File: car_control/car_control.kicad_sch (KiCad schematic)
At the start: 30 parts, among them J1 Screw_Terminal_01x02, J2 Conn_01x03, J3 Conn_01x03, J4 Screw_Terminal_01x02, Q1 IRF540N, Q2 2N3904, SW1 SW_SPST, SW2 SW_Push, U1 TCRT5000

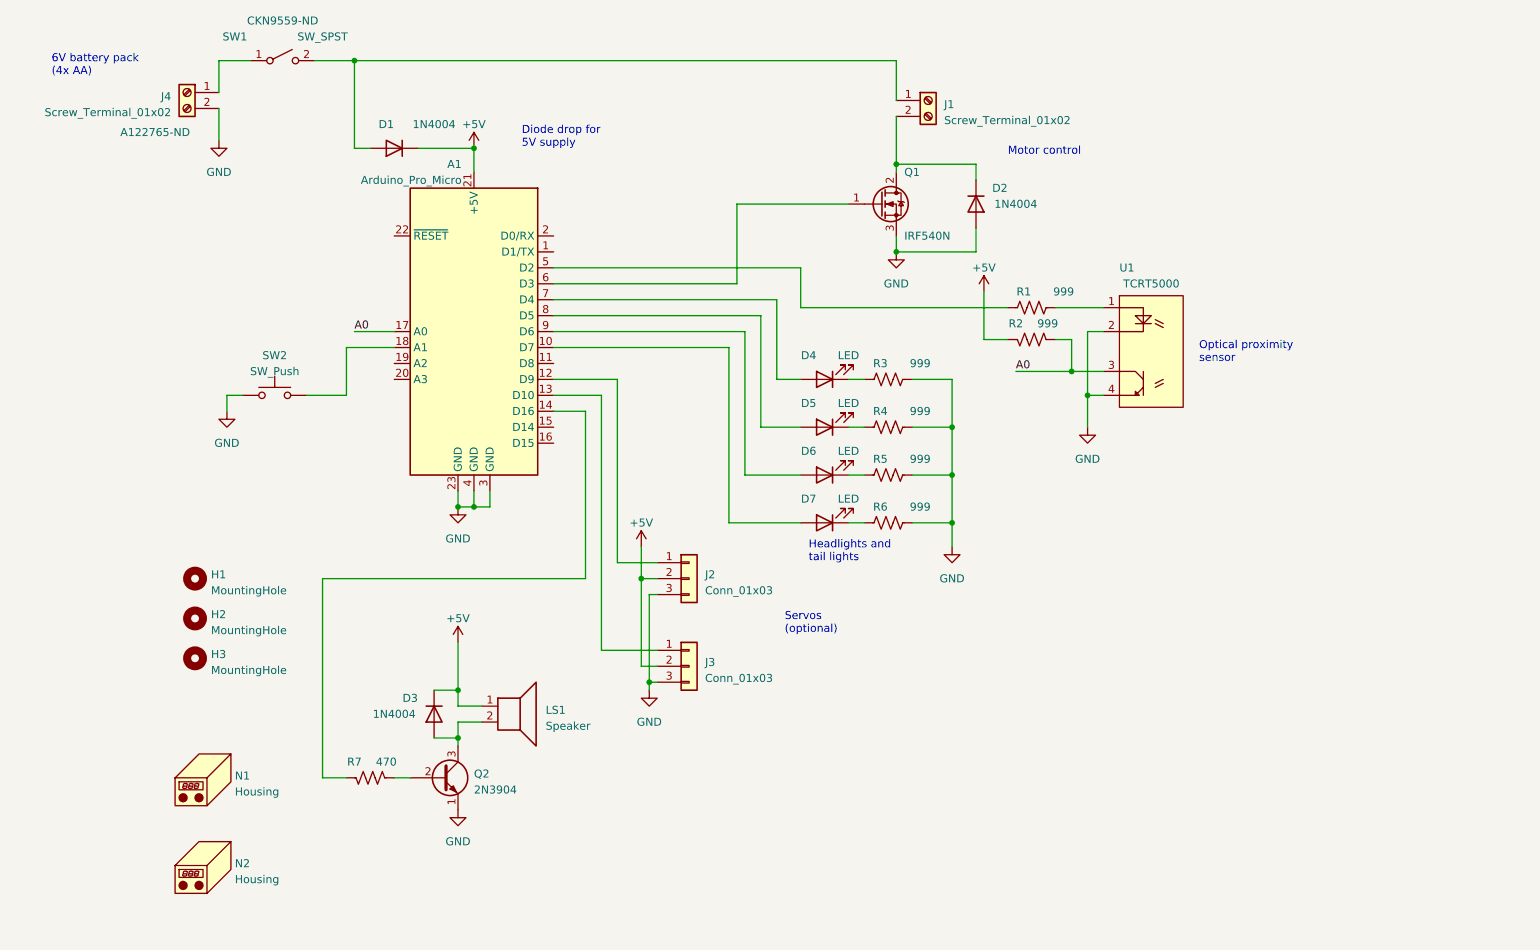
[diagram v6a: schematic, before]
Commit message: Add USB serial connector
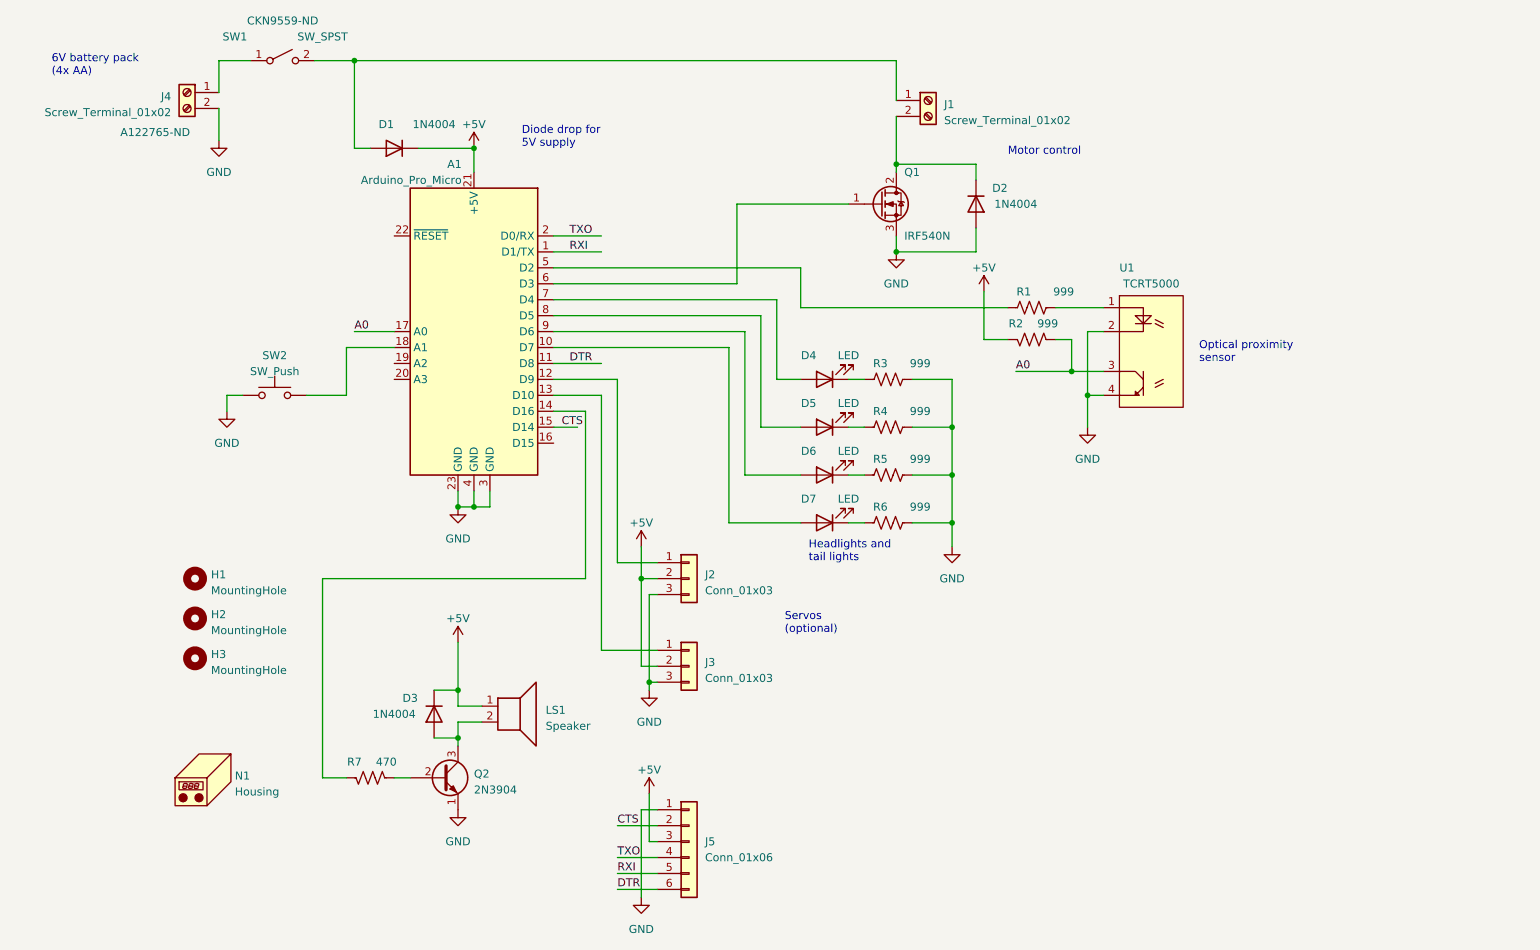
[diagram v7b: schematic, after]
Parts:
- removed N2: Housing, car_as:car_as, symbol Mechanical:Housing
- added J5: Conn_01x06, Connector_PinHeader_2.54mm:PinHeader_1x06_P2.54mm_Vertical, symbol Connector_Generic:Conn_01x06
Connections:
- net +5V: now also J5.3 (Pin_3)
- net GND: now also J5.1 (Pin_1)
- net RXI: now reaches A1.1 (D1/TX)
- net RXI: now also J5.5 (Pin_5)
- net DTR: now reaches A1.11 (D8)
- net DTR: now also J5.6 (Pin_6)
- net CTS: now reaches A1.15 (D14)
- net CTS: now also J5.2 (Pin_2)
- net TXO: now reaches A1.2 (D0/RX)
- net TXO: now also J5.4 (Pin_4)
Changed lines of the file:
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@@
   (junction (at 116.84 146.05) (diameter 0) (color 0 0 0 0)
   )
+  (wire (pts (xy 101.6 95.25) (xy 109.22 95.25))
+    (stroke (width 0) (type default))
+  )
   (wire (pts (xy 148.59 97.79) (xy 151.13 97.79))
     (stroke (width 0) (type default))
@@
     (stroke (width 0) (type default))
   )
+  (wire (pts (xy 116.84 163.83) (xy 116.84 171.45))
+    (stroke (width 0) (type default))
+  )
   (wire (pts (xy 49.53 100.33) (xy 49.53 102.87))
     (stroke (width 0) (type default))
@@
     (stroke (width 0) (type default))
   )
+  (wire (pts (xy 116.84 171.45) (xy 118.11 171.45))
+    (stroke (width 0) (type default))
+  )
   (wire (pts (xy 134.62 105.41) (xy 140.97 105.41))
     (stroke (width 0) (type default))
@@
     (stroke (width 0) (type default))
   )
+  (wire (pts (xy 115.57 166.37) (xy 118.11 166.37))
+    (stroke (width 0) (type default))
+  )
+  (wire (pts (xy 111.76 168.91) (xy 118.11 168.91))
+    (stroke (width 0) (type default))
+  )
+  (wire (pts (xy 101.6 77.47) (xy 109.22 77.47))
+    (stroke (width 0) (type default))
+  )
   (wire (pts (xy 130.81 69.85) (xy 130.81 82.55))
     (stroke (width 0) (type default))
@@
     (stroke (width 0) (type default))
   )
+  (wire (pts (xy 101.6 105.41) (xy 105.41 105.41))
+    (stroke (width 0) (type default))
+  )
   (wire (pts (xy 168.91 66.04) (xy 168.91 63.5))
     (stroke (width 0) (type default))
@@
     (stroke (width 0) (type default))
   )
+  (wire (pts (xy 115.57 180.34) (xy 115.57 166.37))
+    (stroke (width 0) (type default))
+  )
   (wire (pts (xy 69.85 90.17) (xy 76.2 90.17))
     (stroke (width 0) (type default))
@@
     (stroke (width 0) (type default))
   )
+  (wire (pts (xy 111.76 176.53) (xy 118.11 176.53))
+    (stroke (width 0) (type default))
+  )
+  (wire (pts (xy 101.6 74.93) (xy 109.22 74.93))
+    (stroke (width 0) (type default))
+  )
+  (wire (pts (xy 111.76 179.07) (xy 118.11 179.07))
+    (stroke (width 0) (type default))
+  )
   (wire (pts (xy 158.75 120.65) (xy 165.1 120.65))
     (stroke (width 0) (type default))
@@
     (stroke (width 0) (type default))
   )
+  (wire (pts (xy 111.76 173.99) (xy 118.11 173.99))
+    (stroke (width 0) (type default))
+  )
   (wire (pts (xy 111.76 97.79) (xy 111.76 127))
     (stroke (width 0) (type default))
@@
     (effects (font (size 1.27 1.27)) (justify left bottom))
   )
+  (label "DTR" (at 111.76 179.07 0) (fields_autoplaced)
+    (effects (font (size 1.27 1.27)) (justify left bottom))
+  )
+  (label "CTS" (at 111.76 168.91 0) (fields_autoplaced)
+    (effects (font (size 1.27 1.27)) (justify left bottom))
+  )
+  (label "TXO" (at 104.14 74.93 0) (fields_autoplaced)
+    (effects (font (size 1.27 1.27)) (justify left bottom))
+  )
+  (label "TXO" (at 111.76 173.99 0) (fields_autoplaced)
+    (effects (font (size 1.27 1.27)) (justify left bottom))
+  )
+  (label "CTS" (at 102.87 105.41 0) (fields_autoplaced)
+    (effects (font (size 1.27 1.27)) (justify left bottom))
+  )
   (label "A0" (at 175.26 96.52 0) (fields_autoplaced)
+    (effects (font (size 1.27 1.27)) (justify left bottom))
+  )
+  (label "RXI" (at 111.76 176.53 0) (fields_autoplaced)
+    (effects (font (size 1.27 1.27)) (justify left bottom))
+  )
+  (label "DTR" (at 104.14 95.25 0) (fields_autoplaced)
+    (effects (font (size 1.27 1.27)) (justify left bottom))
+  )
+  (label "RXI" (at 104.14 77.47 0) (fields_autoplaced)
     (effects (font (size 1.27 1.27)) (justify left bottom))
   )
@@
     )
   )
+  (symbol (lib_id "power:+5V") (at 116.84 163.83 0) (mirror y) (unit 1)
+    (in_bom yes) (on_board yes) (dnp no) (fields_autoplaced)
+    (property "Reference" "#PWR013" (at 116.84 167.64 0)
+      (effects (font (size 1.27 1.27)) hide)
+    )
+    (property "Value" "+5V" (at 116.84 160.02 0)
+      (effects (font (size 1.27 1.27)))
+    )
+    (property "Footprint" "" (at 116.84 163.83 0)
+      (effects (font (size 1.27 1.27)) hide)
+    )
+    (property "Datasheet" "" (at 116.84 163.83 0)
+      (effects (font (size 1.27 1.27)) hide)
+    )
+    (pin "1")
+    (instances
+      (project "car_control"
+        (path "/08ff0388-b5fa-44e5-b165-5596a9674913"
+          (reference "#PWR013") (unit 1)
+        )
+      )
+    )
+  )
   (symbol (lib_id "Connector_Generic:Conn_01x03") (at 123.19 129.54 0) (unit 1)
     (in_bom yes) (on_board yes) (dnp no) (fields_autoplaced)
@@
     )
   )
-  (symbol (lib_id "Mechanical:Housing") (at 46.99 175.26 0) (unit 1)
-    (in_bom yes) (on_board yes) (dnp no) (fields_autoplaced)
-    (property "Reference" "N2" (at 50.8 174.9425 0)
-      (effects (font (size 1.27 1.27)) (justify left))
-    )
-    (property "Value" "Housing" (at 50.8 177.4825 0)
-      (effects (font (size 1.27 1.27)) (justify left))
-    )
-    (property "Footprint" "car_as:car_as" (at 48.26 173.99 0)
-      (effects (font (size 1.27 1.27)) hide)
-    )
-    (property "Datasheet" "~" (at 48.26 173.99 0)
-      (effects (font (size 1.27 1.27)) hide)
-    )
-    (instances
-      (project "car_control"
-        (path "/08ff0388-b5fa-44e5-b165-5596a9674913"
-          (reference "N2") (unit 1)
-        )
-      )
-    )
-  )
   (symbol (lib_id "Device:R_US") (at 154.94 120.65 90) (unit 1)
     (in_bom yes) (on_board yes) (dnp no)
@@
     )
   )
+  (symbol (lib_id "power:GND") (at 115.57 180.34 0) (unit 1)
+    (in_bom yes) (on_board yes) (dnp no) (fields_autoplaced)
+    (property "Reference" "#PWR014" (at 115.57 186.69 0)
+      (effects (font (size 1.27 1.27)) hide)
+    )
+    (property "Value" "GND" (at 115.57 185.42 0)
+      (effects (font (size 1.27 1.27)))
+    )
+    (property "Footprint" "" (at 115.57 180.34 0)
+      (effects (font (size 1.27 1.27)) hide)
+    )
+    (property "Datasheet" "" (at 115.57 180.34 0)
+      (effects (font (size 1.27 1.27)) hide)
+    )
+    (pin "1")
+    (instances
+      (project "car_control"
+        (path "/08ff0388-b5fa-44e5-b165-5596a9674913"
+          (reference "#PWR014") (unit 1)
+        )
+      )
+    )
+  )
   (symbol (lib_id "Diode:1N4004") (at 82.55 151.13 90) (mirror x) (unit 1)
     (in_bom yes) (on_board yes) (dnp no)
@@
         )
       )
+    )
+  )
+  (symbol (lib_id "Connector_Generic:Conn_01x06") (at 123.19 171.45 0) (unit 1)
+    (in_bom yes) (on_board yes) (dnp no) (fields_autoplaced)
+    (property "Reference" "J5" (at 125.73 171.45 0)
+      (effects (font (size 1.27 1.27)) (justify left))
+    )
+    (property "Value" "Conn_01x06" (at 125.73 173.99 0)
+      (effects (font (size 1.27 1.27)) (justify left))
+    )
+    (property "Footprint" "Connector_PinHeader_2.54mm:PinHeader_1x06_P2.54mm_Vertical" (at 123.19 171.45 0)
+      (effects (font (size 1.27 1.27)) hide)
+    )
+    (property "Datasheet" "~" (at 123.19 171.45 0)
+      (effects (font (size 1.27 1.27)) hide)
+    )
+    (pin "1")
+    (pin "2")
+    (pin "3")
+    (pin "4")
+    (pin "5")
+    (pin "6")
+    (instances
+      (project "car_control"
+        (path "/08ff0388-b5fa-44e5-b165-5596a9674913"
+          (reference "J5") (unit 1)
+        )
+      )

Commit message: Right angle 10mm headlights/tail lights
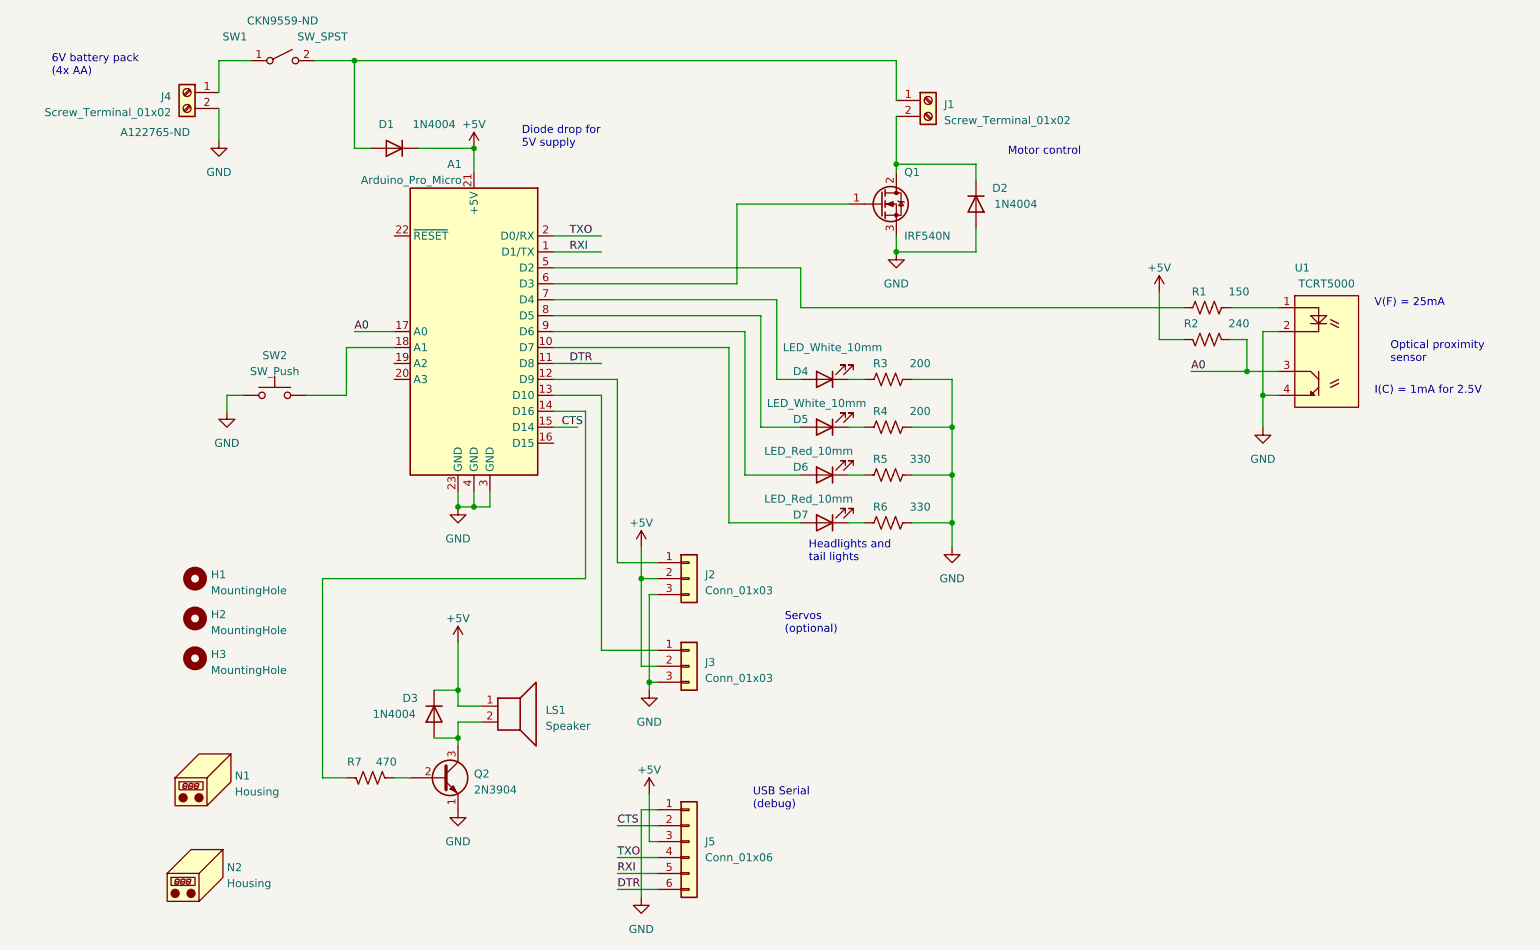
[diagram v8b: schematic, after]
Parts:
- added N2: Housing, car_as:car_as, symbol Mechanical:Housing
- A1, D1, D2, D3, Q1: CatNo (none) -> Amazon (generic)
- D4, D5: value LED -> LED_White_10mm; footprint LED_THT:LED_D3.0mm_Horizontal_O3.81mm_Z2.0mm -> my_10mm_led:LED_D10.0mm_white; CatNo (none) -> Amazon (generic)
- D6, D7: value LED -> LED_Red_10mm; footprint LED_THT:LED_D3.0mm_Horizontal_O3.81mm_Z2.0mm -> my_10mm_led:LED_D10.0mm_red; CatNo (none) -> Amazon (generic)
- J2, J3, J5: CatNo (none) -> DNP
- LS1, SW2, U1: CatNo (none) -> Amazon
- N1: CatNo (none) -> DNP :)
- R1: value 999 -> 150
- R2: value 999 -> 240
- R3, R4: value 999 -> 200
- R5, R6: value 999 -> 330
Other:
- note added: "I(C) = 1mA for 2.5V"
- note added: "USB Serial (debug)"
- note added: "V(F) = 25mA"
- moved on the sheet: R1, R2, U1
